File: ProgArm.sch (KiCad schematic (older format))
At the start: 120 parts, among them J1 MICROSD_SOCKET_SPI, M1 MOTOR, P1 I2C_Port, P2 I2C_Solder, P3 SPI_Port, P4 SPI_Solder, P6 Unused_Pins, P8 Ring_Port, P9 MicroUSB, Q1 MOS_P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

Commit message: Added MPU9250 9-axis sensor
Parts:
- removed C25: 100nF, ~, symbol C
- removed C26: 2n2, ~, symbol C
- removed U5: MPU6050, ~, symbol MPU6050
- added C? (x2): 100nF, ~, symbol C
- added U?: MPU9250, symbol MPU9250
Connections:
- wire segments 459 -> 453
- no-connect marks 4 -> 5
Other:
- note removed: "TODO Replace\nwith MPU9150 (?)"
- moved on the sheet: A?, BT2, C?, JP1, L?, P?, R?, U?, X?

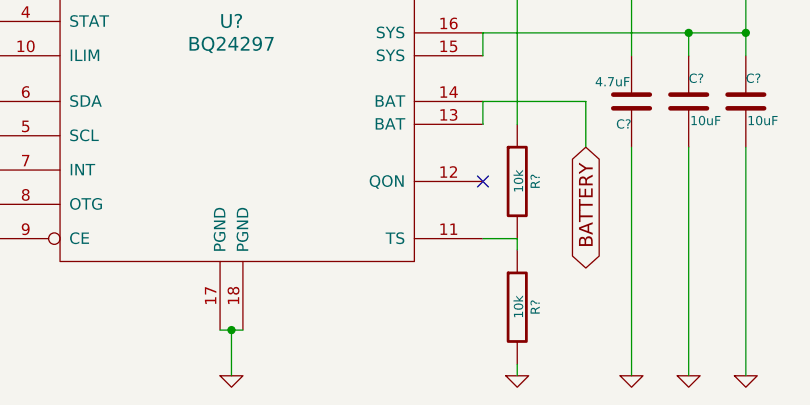
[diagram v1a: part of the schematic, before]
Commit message: added connection for optional thermistor
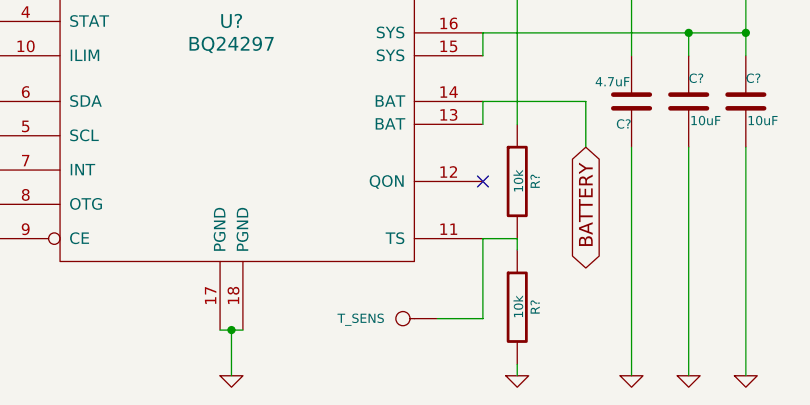
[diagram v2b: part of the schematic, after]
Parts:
- added T_SENS: CONN_1, symbol CONN_1
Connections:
- wire segments 453 -> 455
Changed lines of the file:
@@
 	1    0    0    -1
 $EndComp
+$Comp
+L CONN_1 T_SENS
+U 1 1 547B9461
+P 4100 10750
+F 0 "T_SENS" H 4180 10750 40  0000 L CNN
+F 1 "CONN_1" H 4100 10805 30  0001 C CNN
+F 2 "" H 4100 10750 60  0000 C CNN
+F 3 "" H 4100 10750 60  0000 C CNN
+	1    4100 10750
+	-1   0    0    1
+$EndComp
+Wire Wire Line
+	4450 10400 4450 10750
+Wire Wire Line
+	4450 10750 4250 10750
 $EndSCHEMATC

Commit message: Replaced nRF51 series chip with nRF8001; removed SD_CARD
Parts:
- removed A?: ANT, ~, symbol ANT
- removed C?: 47uF, ~, symbol C
- removed C?: 2.2nF, ~, symbol C
- removed C?: 1.0nF, ~, symbol C
- removed C?: 2.2pF, ~, symbol C
- removed C?: 1.0pF, ~, symbol C
- removed C?: 1.5pF, ~, symbol C
- removed C? (x2): 100nF, ~, symbol C
- removed C?: 4.7uF, ~, symbol C
- removed C?: 1uF, ~, symbol C
- removed C? (x2): 12pF, ~, symbol C
- removed J1: MICROSD_SOCKET_SPI, ~, symbol MICROSD_SOCKET_SPI
- removed L?: 10nH, ~, symbol INDUCTOR
- removed L?: 4.7nH, ~, symbol INDUCTOR
- removed L?: 3.3nH, ~, symbol INDUCTOR
- removed L?: 10uH, ~, symbol INDUCTOR
- removed L?: 15nH, ~, symbol INDUCTOR
- removed P?: BT_SWD, symbol CONN_4
- removed Q3: MOS_N, ~, symbol MOS_N
- removed Q4: MOS_P, ~, symbol MOS_P
- removed R14: 100k, ~, symbol R
- removed R16: 300R, ~, symbol R
- removed SW2: SWITCH_INV, ~, symbol SWITCH_INV
- removed U?: NRF51822, ~, symbol NRF51822
- removed X?: 32.768kHz, ~, symbol CRYSTAL
- added A?: ANT, ~, symbol ANT
- added B?: 8001_BALUN, symbol 8001_BALUN
- added C?: 1uF, ~, symbol C
- added C?: 2.2nF, ~, symbol C
- added C?: 4.7uF, ~, symbol C
- added C?: 100nF, ~, symbol C
- added C?: 33nF, ~, symbol C
- added L?: 15nH, ~, symbol INDUCTOR
- added L?: 10uH, ~, symbol INDUCTOR
- added R?: 22k, ~, symbol R
- added R? (x5): 10k, ~, symbol R
- added RXD, TXD: CONN_1, symbol CONN_1
- added U?: NRF8001, symbol NRF8001
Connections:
- net labels added: BT_MISO, BT_MOSI, BT_SCK, ~RDYN, ~REQN
- net labels removed: BT_AVDD, BT_POWER, BT_RXTX, BT_TXRX, CLK, FW/RST, IO, SD_CD, SD_MISO, SD_MOSI, SD_NSS, SD_SCK, ~BT_PWR_ENABLE, ~SYS_PWR_ENABLE
- wire segments 455 -> 442
- no-connect marks 5 -> 10
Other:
- moved on the sheet: C?, Q5, R15, R17, X?

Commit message: Added  IR LED and Sensor connections for ring port
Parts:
- removed BZ1: PIEZZO, ~, symbol BUZZER_A
- removed P8: Ring_Port, symbol CONN_6
- removed Q12: MOS_P, ~, symbol MOS_P
- removed R26, R35: 10k, ~, symbol R
- removed R29: 300R, ~, symbol R
- added Q?: MOS_P, ~, symbol MOS_P
- added R?: 10k, ~, symbol R
- added R?: 300R, ~, symbol R
- added RING_PORT: CONN_9, symbol CONN_9
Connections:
- net +3.3V: now also Q?.2 (S), R?.1, RING_PORT.1 (P1)
- net GND: now also RING_PORT.9 (P9)
- net ~RING_BTN2: now also RING_PORT.4 (P4)
- net at Q10.1 (G), R27.1: now also RING_PORT.2 (P2)
- net at Q7.3 (D): now also RING_PORT.5 (P5)
- net at Q8.3 (D): now also RING_PORT.6 (P6)
- net at Q9.3 (D): now also RING_PORT.7 (P7)
- net ~LED_IR: now reaches U1.20 (SPI1_NSS/ADC1_IN4/USART2_CK/DAC1_OUT/PA4)
- net ~LED_IR: now also R?.2
- net IR_SIGNAL: now reaches U1.41 (USART1_CK/MCO/TIM1_CH1/PA8)
- net IR_SIGNAL: now also RING_PORT.3 (P3)
- net in_current renamed IN_CURRENT
- new net: Q?.3 (D), RING_PORT.8 (P8)
- new net: Q?.1 (G), R?.1, R?.2
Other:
- moved on the sheet: C3, C4, D3, M1, P6, Q10, Q11, Q5, Q7, Q8, Q9, R15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

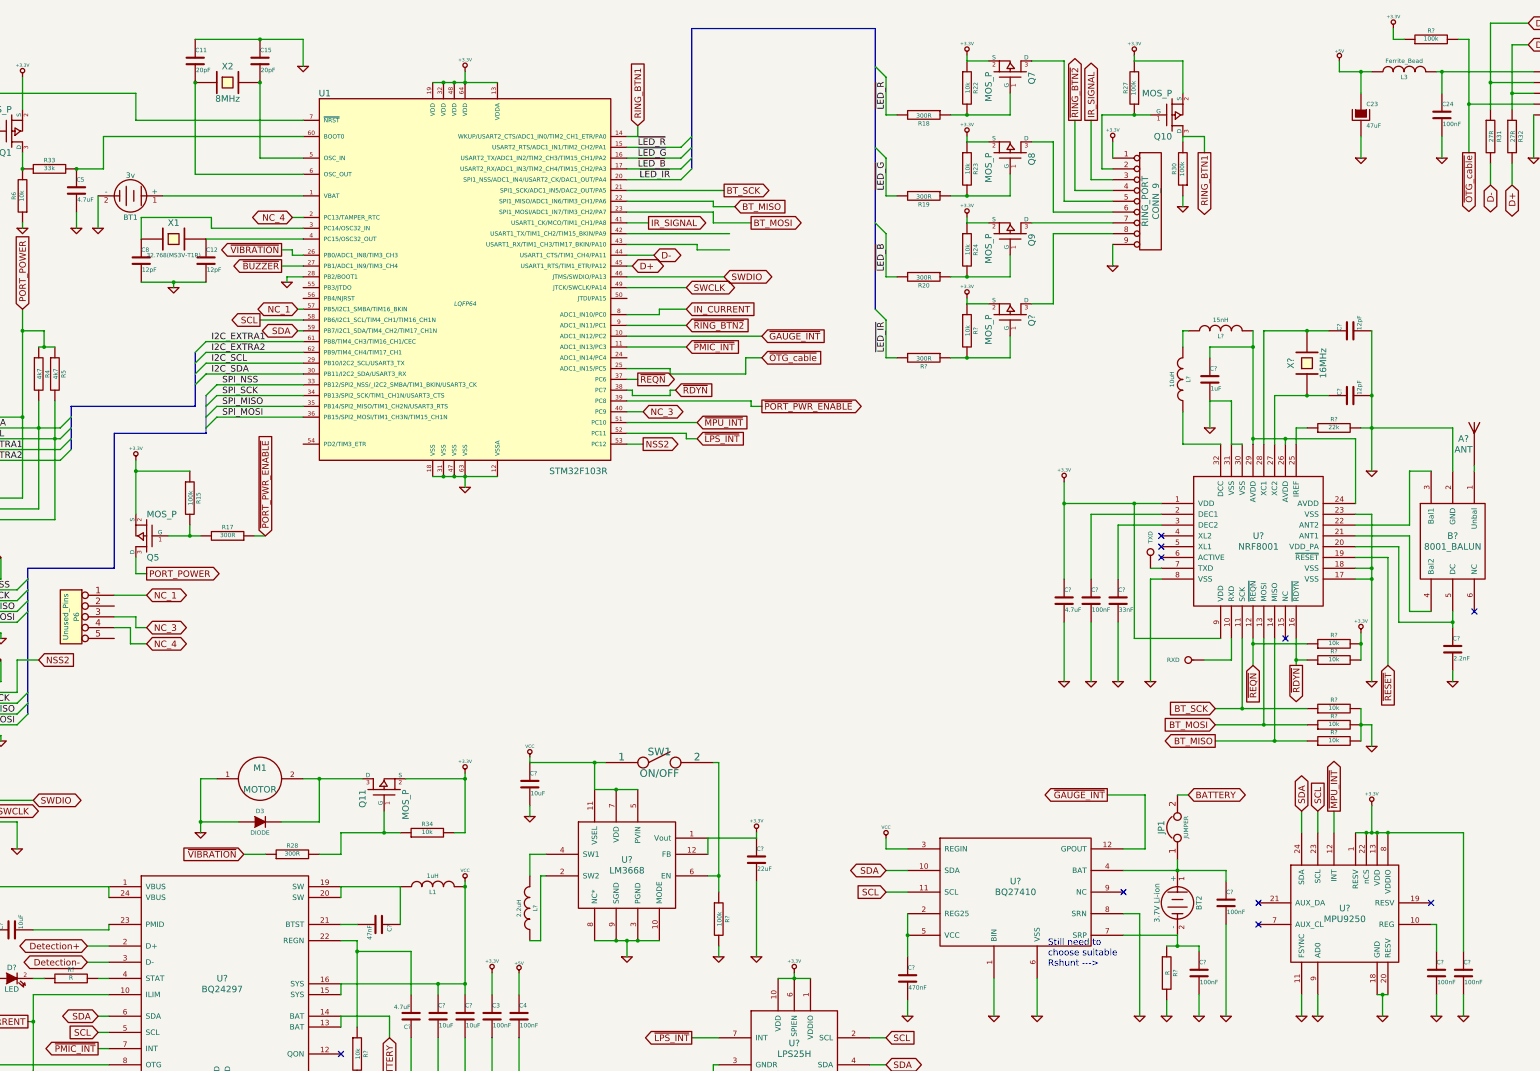
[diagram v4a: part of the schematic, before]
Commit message: Added Ionistor backup instead of battery
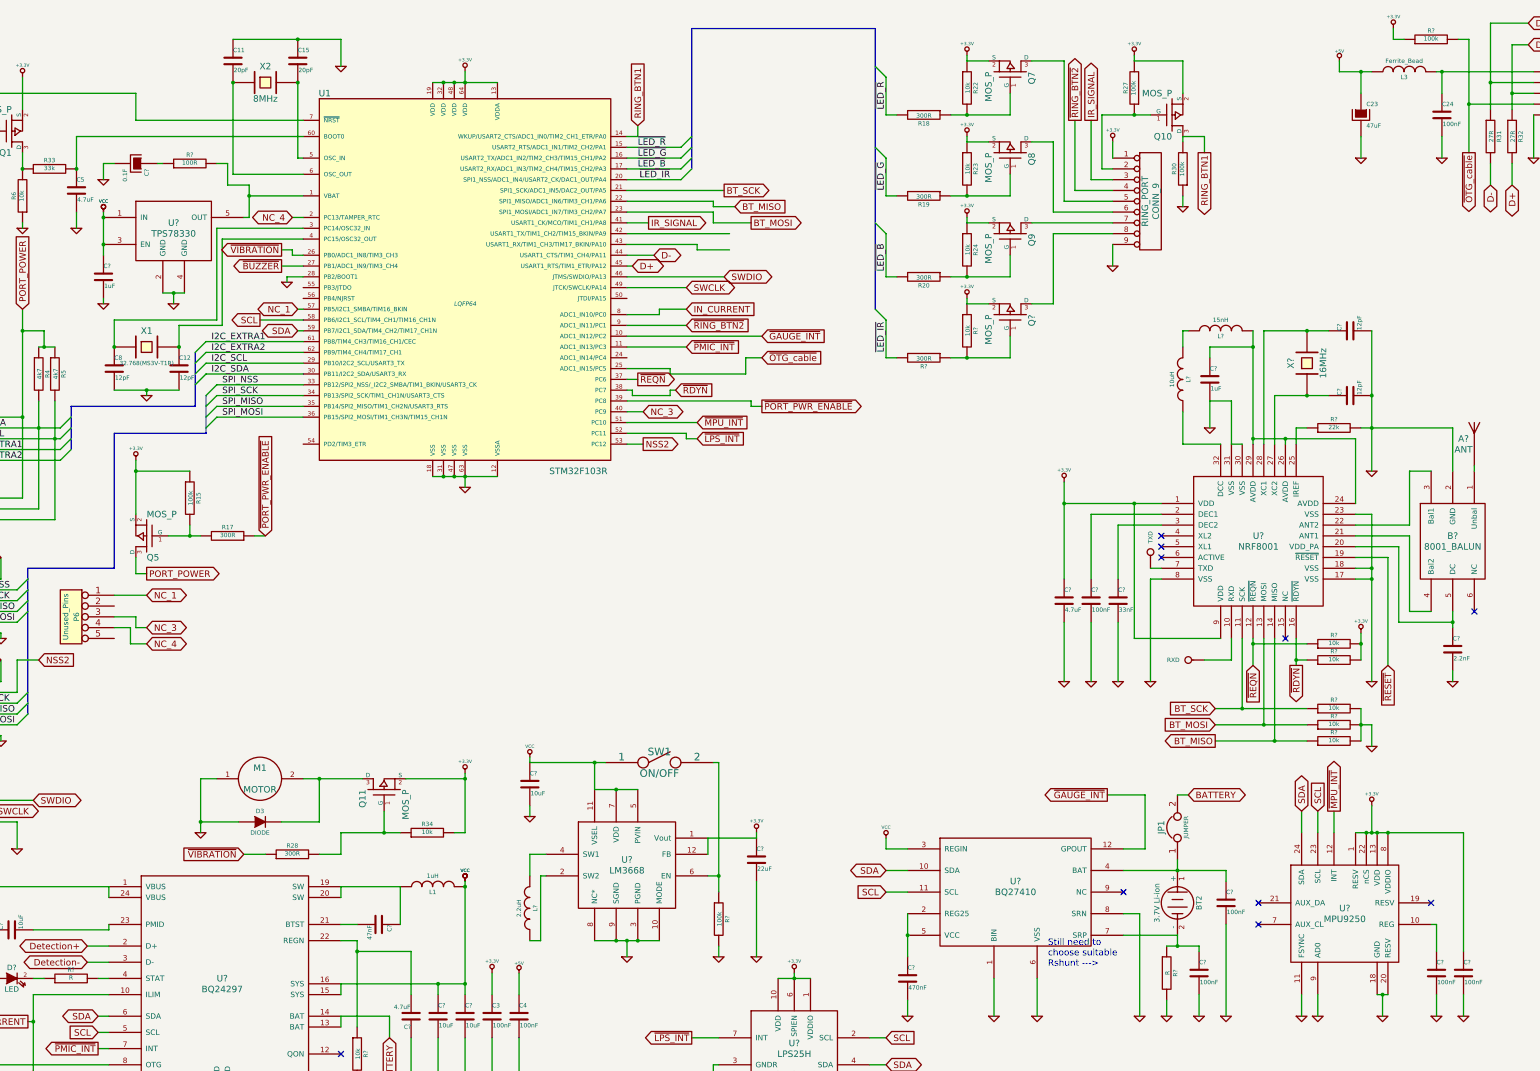
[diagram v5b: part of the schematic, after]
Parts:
- removed BT1: 3v, ~, symbol BATTERY
- added C?: 1uF, ~, symbol C
- added C?: 0.1F, ~, symbol CAPAPOL
- added R?: 100R, ~, symbol R
- added U?: TPS78330, ~, symbol TPS78330
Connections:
- net GND: now also C?.2, C?.2, U?.2 (GND), U?.4 (GND)
- net VCC: now also C?.1, U?.1 (IN), U?.3 (EN)
- net at U1.1 (VBAT): now also R?.2, U?.5 (OUT)
- new net: C?.1, R?.1
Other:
- moved on the sheet: C11, C12, C15, C8, X1, X2

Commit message: Added Si1143-based Pulse Meter
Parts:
- added C?: 100nF, ~, symbol C
- added C? (x2): 22uF, ~, symbol C
- added D? (x3): LED, ~, symbol LED
- added R?: 4.7k, ~, symbol R
- added R?: 47k, ~, symbol R
- added R?: 30R, ~, symbol R
- added U?: SI1143, symbol SI1143
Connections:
- net +3.3V: now also C?.1, R?.1, R?.1, R?.1, U?.3 (VDD)
- net GND: now also C?.2, C?.2, C?.2, U?.8 (GND)
- net SCL: now also U?.2 (SCL)
- net SDA: now also U?.1 (SDA)
- net ~SI_INT: now reaches U1.24 (ADC1_IN14/PC4)
- net ~SI_INT: now also R?.2, U?.4 (INT)
- new net: D?.2 (K), U?.6 (LED2)
- new net: D?.2 (K), R?.2, U?.7 (LED3)
- new net: D?.2 (K), U?.9 (LED1)
- new net: C?.1, C?.1, D?.1 (A), D?.1 (A), D?.1 (A), R?.2

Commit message: Removed useless elements (buzzer signals, solder ports, NC pins etc.)
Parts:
- removed P2: I2C_Solder, symbol CONN_4
- removed P4: SPI_Solder, symbol CONN_6
- removed P6: Unused_Pins, symbol CONN_5
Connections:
- net NC_1: no longer names the net of U1.57 (PB5/I2C1_SMBA/TIM16_BKIN)
- net NC_3: no longer names the net of U1.40 (PC9)
- net NC_4: no longer names the net of U1.2 (PC13/TAMPER_RTC)
- net NSS2: no longer names the net of U1.53 (PC12)
- net ~BUZZER: no longer names the net of U1.27 (PB1/ADC1_IN9/TIM3_CH4)

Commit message: Removed unused third LED in the pulse sensor schematic
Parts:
- removed D?: LED, ~, symbol LED
- removed R?: 47k, ~, symbol R
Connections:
- net +3.3V: now also U?.7 (LED3)
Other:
- moved on the sheet: D?
